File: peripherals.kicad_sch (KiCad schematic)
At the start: 21 parts, among them J14 GPIO_Expander, J15 LED 5V, U17 TCAL9539RTWRQ1, U18 WS2816B, U19 SN74LV1T34DCK, U2 QMC6309, U20 WS2816B, U22 LSM6DSV16X, U24 TPD2E2U06QDCKRQ1

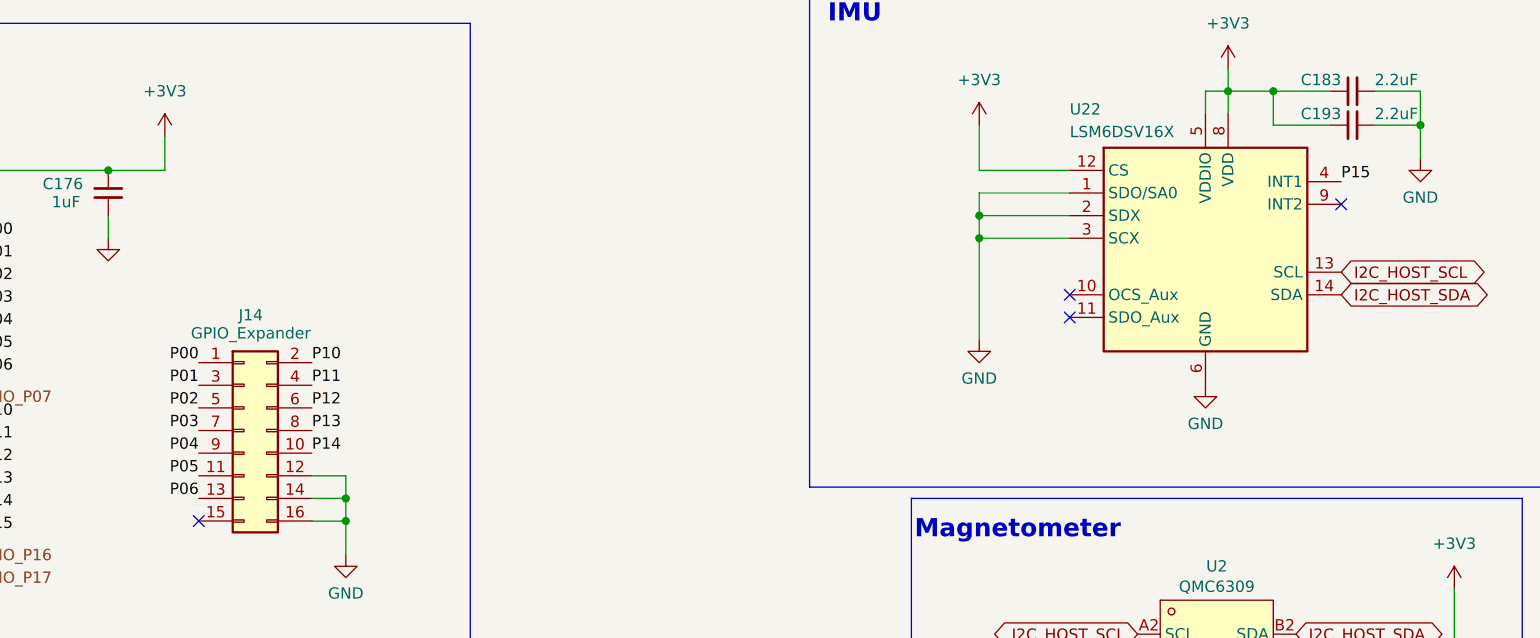
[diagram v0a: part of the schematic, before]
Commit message: board: route 6 of the last 7 links; move D3, U22 cluster, FID2; swap P05/P15
- D3 (UART0 ESD) moves to F.Cu under J6 (was 26.7 mm away on B.Cu); UART0
  RAW stubs now ~5 mm each (TX was 45 mm), UART0_TX/RX re-laid at ~16 mm.
  FID2 moves to 99.6,157.7 to make room.
- U22 (LSM6DSV16X) + C183/C193 move from the boxed-in B.Cu hole under U1's
  corner to F.Cu west of U1 (100.9,152.8 r180); all their nets routed.
- Schematic: U22 INT1 now on TCAL9539 P05, J14.11 on P15 (U17.15's west face
  has no via access). Two label renames; knet diff = 4 pins, ERC unchanged.
- C_SBU2 (J7.B8 -> U4.2) and the J4/D28 I2C_HOST_SDA group routed.
- KiCad DRC vs the pre-change baseline: 0 new, 1 gone; unconnected 7 -> 1.
  Still open: GPIO_38 (R4.1 -> U1.31), boxed in at R4 and with no path off
  the antenna area.

Co-Authored-By: Claude Opus 5.5 <noreply@anthropic.com>
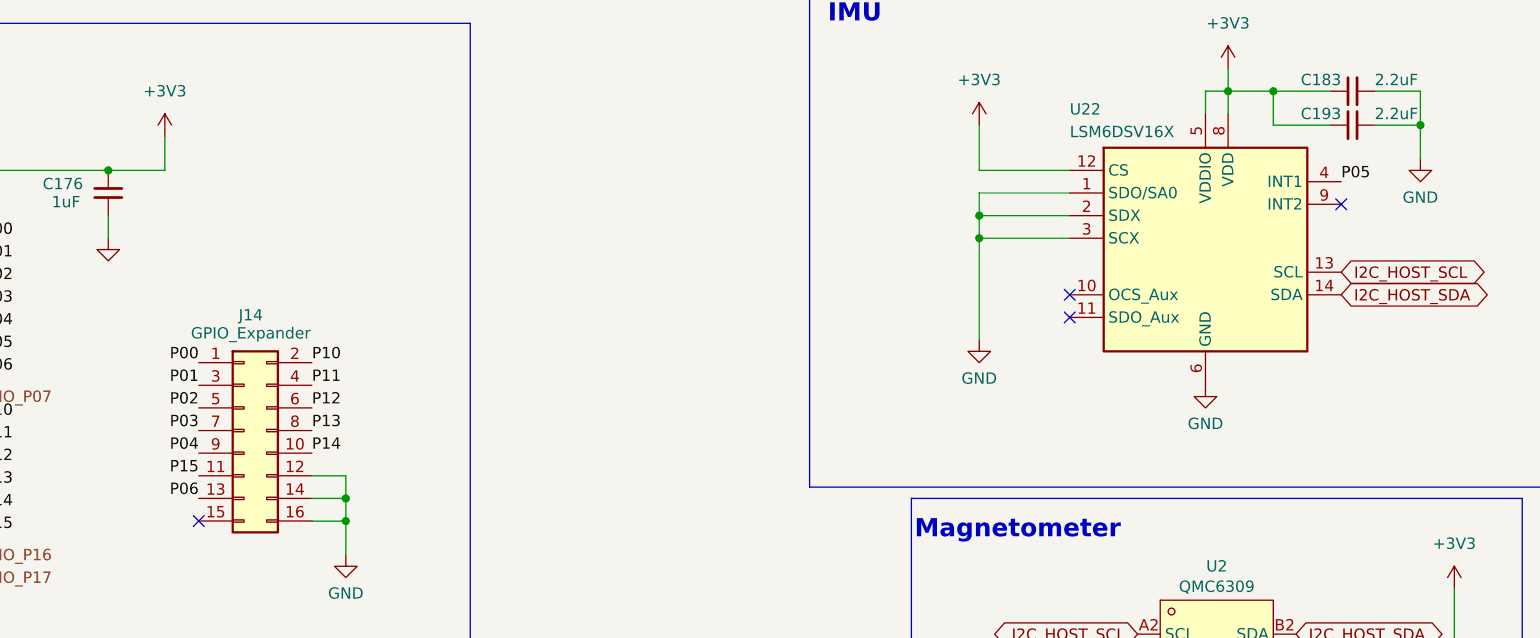
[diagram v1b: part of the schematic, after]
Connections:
- net P05: now also U22.4 (INT1); no longer J14.11 (Pin_11)
- net P15: now also J14.11 (Pin_11); no longer U22.4 (INT1)
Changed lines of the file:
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@@
 		)
 	)
-	(label "P15"
+	(label "P05"
 		(at 250.19 86.36 0)
 		(effects
@@
 		)
 	)
-	(label "P05"
+	(label "P15"
 		(at 121.92 119.38 180)
 		(effects
